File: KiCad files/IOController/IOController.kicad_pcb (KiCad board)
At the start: 2 copper layers, 22.5 x 68.6 mm, 31 parts, among them J1 AVR-ISP-6, J3 XT60 Horizontal Socket, J6 XT60 Horizontal Socket, Q1 BSS138, SW1 RotaryEncoder_Switch, SW2 SW_Push, U1 ATtiny85-20P, U3 LP2985-1.8, U4 LP2985-5.0

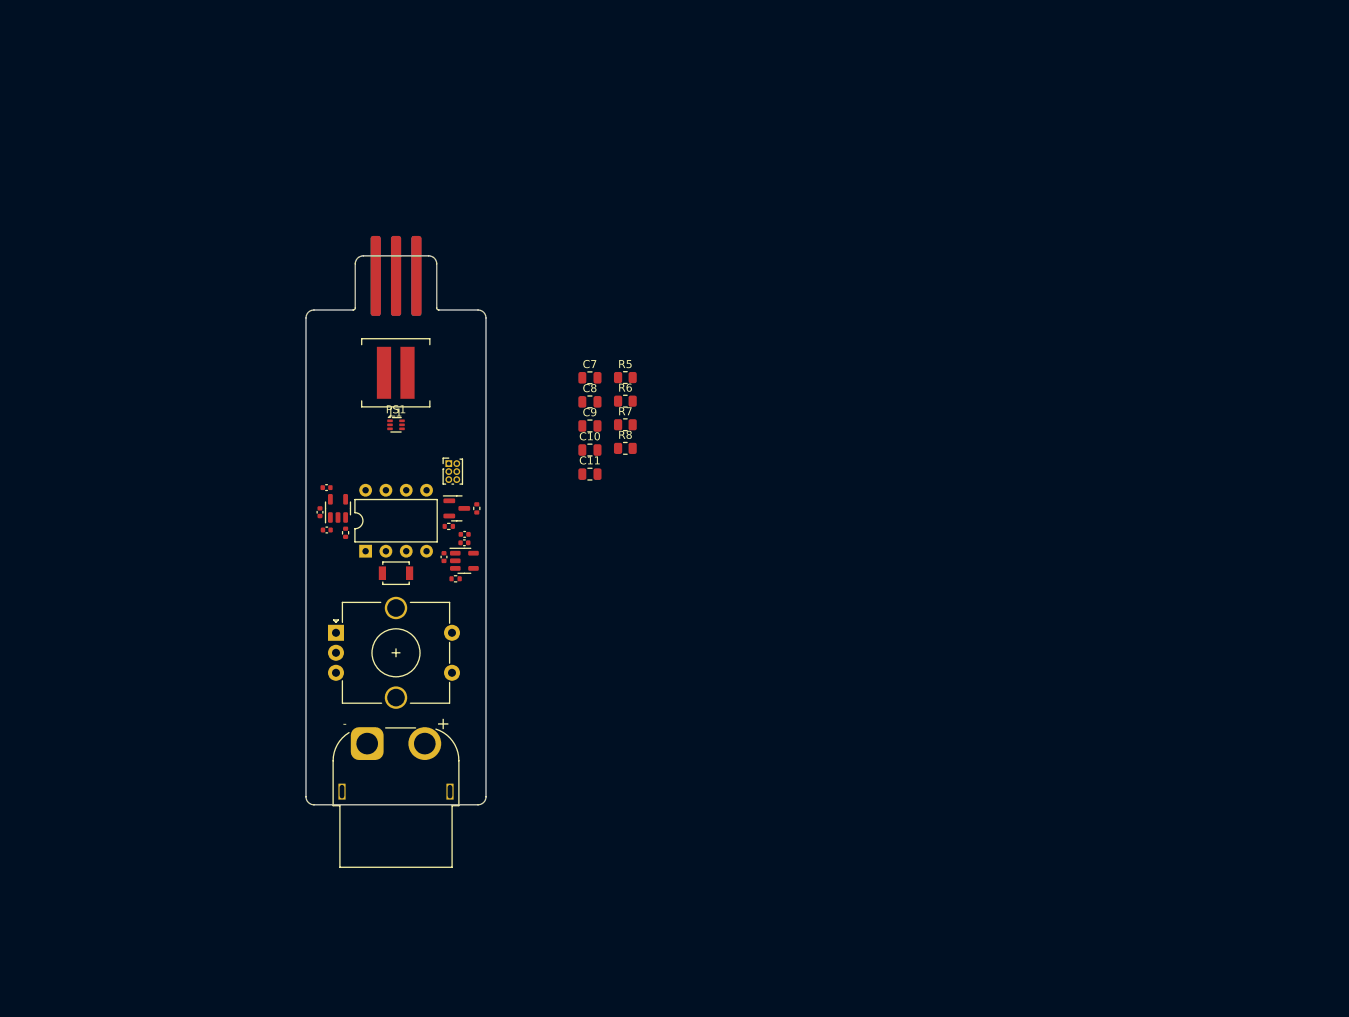
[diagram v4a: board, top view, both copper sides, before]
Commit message: started re-work of led driver circuit on IO board
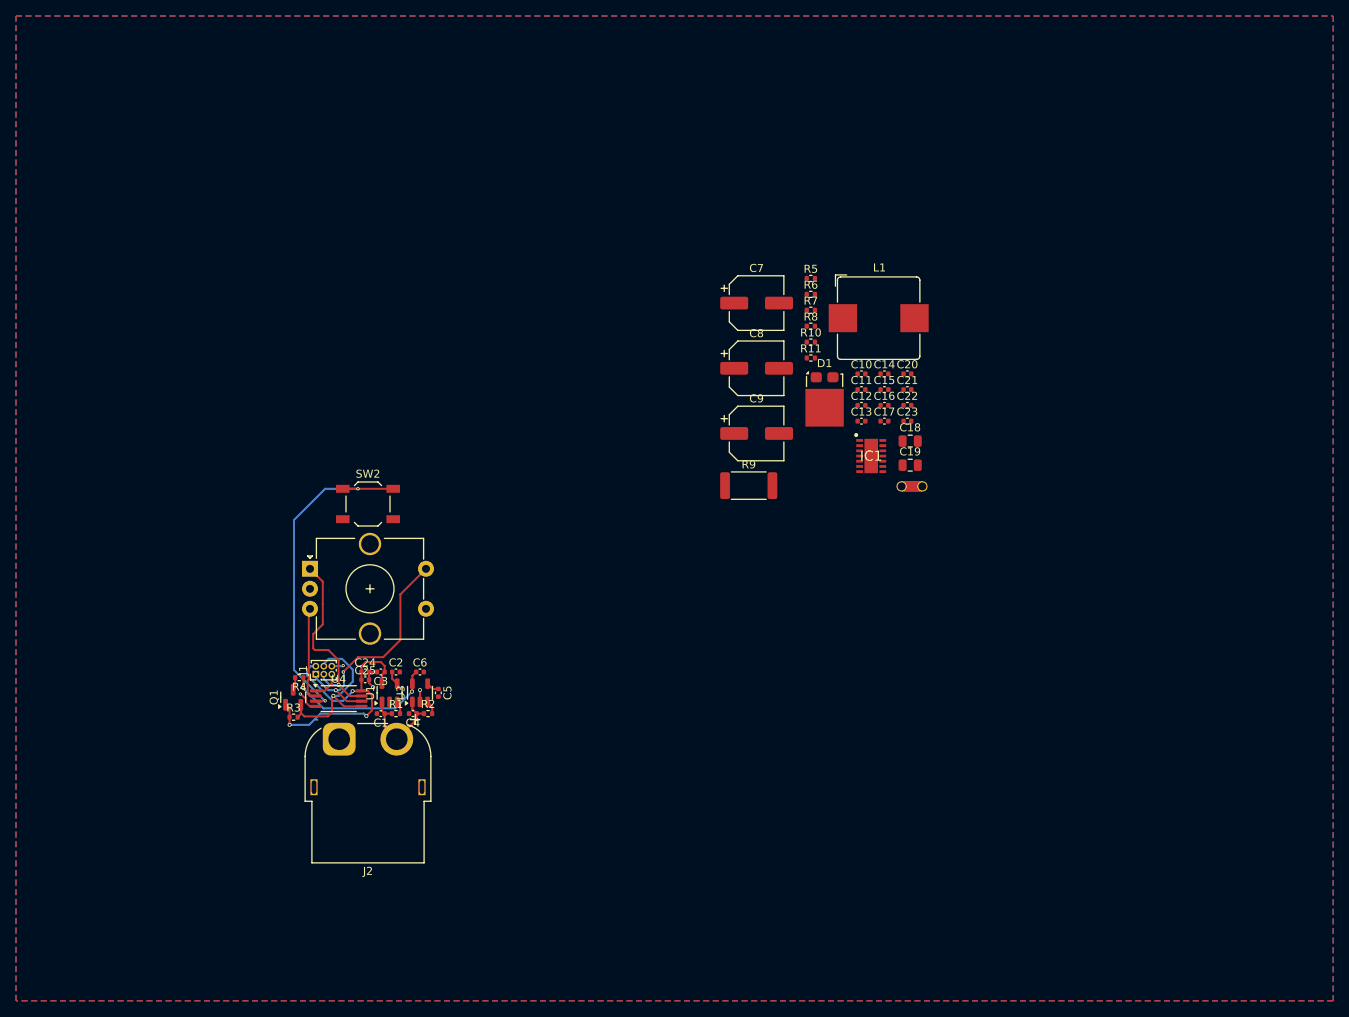
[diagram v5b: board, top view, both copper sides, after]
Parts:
- removed J3: XT60 Horizontal Socket, Connector_AMASS:AMASS_XT60PW-F_1x02_P7.20mm_Horizontal
- removed J6 (x2): XT60 Horizontal Socket, Connector_PinHeader_2.54mm:PinHeader_1x03_P2.54mm_Vertical
- removed PS1: TPS566242DRLR, Package_TO_SOT_SMD:SOT-563
- added C12: 25V 1uF 0402, Capacitor_SMD:C_0402_1005Metric, F.Cu at (90.7, 51.1)
- added C13: 25V 1uF 0402, Capacitor_SMD:C_0402_1005Metric, F.Cu at (90.7, 53.0)
- added C14: 25V 100nF 0402, Capacitor_SMD:C_0402_1005Metric, F.Cu at (93.6, 47.1)
- added C15: 10V 10nF 0402, Capacitor_SMD:C_0402_1005Metric, F.Cu at (93.6, 49.1)
- added C16: 10V 10nF 0402, Capacitor_SMD:C_0402_1005Metric, F.Cu at (93.6, 51.1)
- added C17: 16V 2.2uF 0402, Capacitor_SMD:C_0402_1005Metric, F.Cu at (93.6, 53.0)
- added C18: 50V 2.2uF 0805, Capacitor_SMD:C_0805_2012Metric, F.Cu at (96.8, 55.5)
- added C19: 50V 2.2uF 0805, Capacitor_SMD:C_0805_2012Metric, F.Cu at (96.8, 58.5)
- added C20: 50V 1uF 0402, Capacitor_SMD:C_0402_1005Metric, F.Cu at (96.4, 47.1)
- added C21: 50V 1uF 0402, Capacitor_SMD:C_0402_1005Metric, F.Cu at (96.4, 49.1)
- added C22: 50V 100nF 402, Capacitor_SMD:C_0402_1005Metric, F.Cu at (96.4, 51.1)
- added C23: 50V 100nF 402, Capacitor_SMD:C_0402_1005Metric, F.Cu at (96.4, 53.0)
- added C24: 0.1uF 0402, Capacitor_SMD:C_0402_1005Metric, F.Cu at (28.7, 84.4)
- added C25: 1uF 0402, Capacitor_SMD:C_0402_1005Metric, F.Cu at (28.7, 85.4)
- added D1: FSV12100V, Package_TO_SOT_SMD:TO-277A, F.Cu at (86.1, 50.3)
- added IC1: TPS922054DMTR, TPS922054DMTR:SON65P300X450X100-15N-D, F.Cu at (91.9, 57.4)
- added J2: XT60 Horizontal Socket, Connector_AMASS:AMASS_XT60PW-F_1x02_P7.20mm_Horizontal, F.Cu at (25.4, 92.8)
- added NTe1: NetTie_2, NetTie:NetTie-2_THT_Pad1.0mm, F.Cu at (95.7, 61.2)
- added R10: 309K 0402, Resistor_SMD:R_0402_1005Metric, F.Cu at (84.4, 43.2)
- added R11: 102K 0402, Resistor_SMD:R_0402_1005Metric, F.Cu at (84.4, 45.2)
- added R9: 33mΩ 2512, Resistor_SMD:R_2512_6332Metric, F.Cu at (76.6, 61.1)
- C1, C4: value 0402 1uF -> 1uF 0402
- C10: value 22uF -> 50V 100nF 402; footprint Capacitor_SMD:C_0805_2012Metric -> Capacitor_SMD:C_0402_1005Metric
- C11: value 100nF -> 50V 100nF 402; footprint Capacitor_SMD:C_0805_2012Metric -> Capacitor_SMD:C_0402_1005Metric
- C2, C5: value 0402 10nF -> 10nF 0402
- C3, C6: value 0402 2.2uF -> 2.2uF 0402
- C7: value 10uF 0805 -> 50V 68uF D6.3; footprint Capacitor_SMD:C_0805_2012Metric -> Capacitor_SMD:CP_Elec_6.3x5.9
- C8: value 100nF 0805 -> 50V 22uF D6.3; footprint Capacitor_SMD:C_0805_2012Metric -> Capacitor_SMD:CP_Elec_6.3x5.9
- C9: value 100nF -> 50V 22uF D6.3; footprint Capacitor_SMD:C_0805_2012Metric -> Capacitor_SMD:CP_Elec_6.3x5.9
- L1: value MDA7030-2R2M -> 10uH SRP1038WA; footprint Inductor_SMD:L_Coilcraft_XAL7030-222 -> Inductor_SMD:L_Bourns_SRP1038C_10.0x10.0mm
- R5: value 100K 0805 -> 10K 0402; footprint Resistor_SMD:R_0805_2012Metric -> Resistor_SMD:R_0402_1005Metric
- R6: value 23.2K 0805 -> 52K3 0402; footprint Resistor_SMD:R_0805_2012Metric -> Resistor_SMD:R_0402_1005Metric
- R7: value 120K 0805 -> 61K9 0402; footprint Resistor_SMD:R_0805_2012Metric -> Resistor_SMD:R_0402_1005Metric
- R8: value 30K 0805 -> 825ohm 0402; footprint Resistor_SMD:R_0805_2012Metric -> Resistor_SMD:R_0402_1005Metric
- SW2: value SW_Push -> TL3342; footprint Button_Switch_SMD:SW_SPST_B3U-1000P -> Button_Switch_SMD:SW_SPST_TL3342
- U1: value ATtiny85-20P -> LP2985-1.8; footprint Package_DIP:DIP-8_W7.62mm -> Package_TO_SOT_SMD:SOT-23-5
- U3: value LP2985-1.8 -> LP2985-5.0
- U4: value LP2985-5.0 -> ATtiny45V-10X; footprint Package_TO_SOT_SMD:SOT-23-5 -> Package_SO:TSSOP-8_4.4x3mm_P0.65mm
- moved L1 60.8 mm to (92.8, 40.2), turned to 0 degrees
- moved C11 35.5 mm to (90.7, 49.1)
- moved C10 35.3 mm to (90.7, 47.1)
- moved Q1 31.2 mm to (19.6, 87.6), turned to 90 degrees
- moved J1 31.1 mm to (22.5, 84.7), turned to 90 degrees
- moved R3 30.7 mm to (19.7, 90.0)
- moved R4 30.7 mm to (20.4, 85.1), turned to 180 degrees
- moved R8 27.8 mm to (84.4, 41.2)
- moved R7 27.2 mm to (84.4, 39.2)
- moved R6 26.8 mm to (84.4, 37.2)
- moved R5 26.3 mm to (84.4, 35.2)
- moved U3 25.2 mm to (35.5, 87.0)
- moved C3 24.0 mm to (30.6, 84.4)
- moved C1 23.9 mm to (30.6, 89.6)
- moved R1 23.5 mm to (32.5, 89.6), turned to 0 degrees
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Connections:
- net NPN-Gate_5V renamed LED_PWM_5V
- C10 pad 1: VDD -> VCC
- C10 pad 2: GND -> GNDPWR
- C11 pad 1: VDD -> VCC
- C11 pad 2: GND -> GNDPWR
- C2 pad 1: Net-(U3-BP) -> Net-(U1-BP)
- C5 pad 1: Net-(U4-BP) -> Net-(U3-BP)
- C7 pad 2: GND -> GNDPWR
- C8 pad 2: GND -> GNDPWR
- C9 pad 1: VDD -> VCC
- C9 pad 2: Net-(PS1-FB) -> GNDPWR
- J1 pad 4: NPN-Gate_1.8V -> LED_PWM_1V8
- L1 pad 2: VDD -> Net-(IC1-CSN)
- Q1 pad 2: NPN-Gate_1.8V -> LED_PWM_1V8
- R1 pad 2: Net-(U3-ON/~{OFF}) -> Net-(U1-ON/~{OFF})
- R2 pad 2: Net-(U4-ON/~{OFF}) -> Net-(U3-ON/~{OFF})
- R3 pad 2: NPN-Gate_1.8V -> LED_PWM_1V8
- R5 pad 1: Net-(PS1-EN) -> VCC
- R5 pad 2: VCC -> Net-(IC1-ADIM/HD)
- R6 pad 1: Net-(PS1-EN) -> Net-(IC1-FSET)
- R7 pad 1: VDD -> Net-(IC1-TEMP)
- R7 pad 2: Net-(PS1-FB) -> GND
- R8 pad 1: Net-(PS1-FB) -> Net-(IC1-COMP)
- R8 pad 2: GND -> Net-(C15-Pad1)
- U1 pad 1: Net-(J1-~{RST}) -> VCC
- U1 pad 2: ROT_B -> GND
- U1 pad 3: SW1 -> Net-(U1-ON/~{OFF})
- U1 pad 4: GND -> Net-(U1-BP)
- U1 pad 5: NPN-Gate_1.8V -> +1V8
- U3 pad 5: +1V8 -> +5V
- U4 pad 1: VCC -> Net-(J1-~{RST})
- U4 pad 2: GND -> ROT_B
- U4 pad 3: Net-(U4-ON/~{OFF}) -> SW1
- U4 pad 4: Net-(U4-BP) -> GND
- U4 pad 5: +5V -> LED_PWM_1V8
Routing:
- net SW1: track 0.00 -> 43.3 mm, vias 0 -> 2
- net +1V8: track 0.00 -> 36.8 mm, vias 0 -> 3
- net ROT_SW1: track 0.00 -> 29.4 mm, vias 0 -> 2
- net ROT_A: track 0.00 -> 24.2 mm, vias 0 -> 1
- net LED_PWM_1V8: track 0.00 -> 22.6 mm, vias 0 -> 1
- net +5V: track 0.00 -> 19.5 mm, vias 0 -> 2
- net VCC: track 0.00 -> 13.2 mm
- net ROT_B: track 0.00 -> 11.9 mm
- net GND: track 0.00 -> 8.85 mm, vias 0 -> 4
- net Net-(J1-~{RST}): track 0.00 -> 3.56 mm
- net Net-(U1-BP): track 0.00 -> 1.72 mm
- net Net-(U3-ON/~{OFF}): track 0.00 -> 1.70 mm
- net LED_PWM_5V: track 0.00 -> 1.63 mm
- net Net-(U3-BP): track 0.00 -> 1.62 mm
- net Net-(U1-ON/~{OFF}): track 0.00 -> 1.61 mm
- added copper zone on B.Cu, net GND
- added copper zone on F.Cu, net GND
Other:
- board outline removed

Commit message: completed circuit, could be laid out better
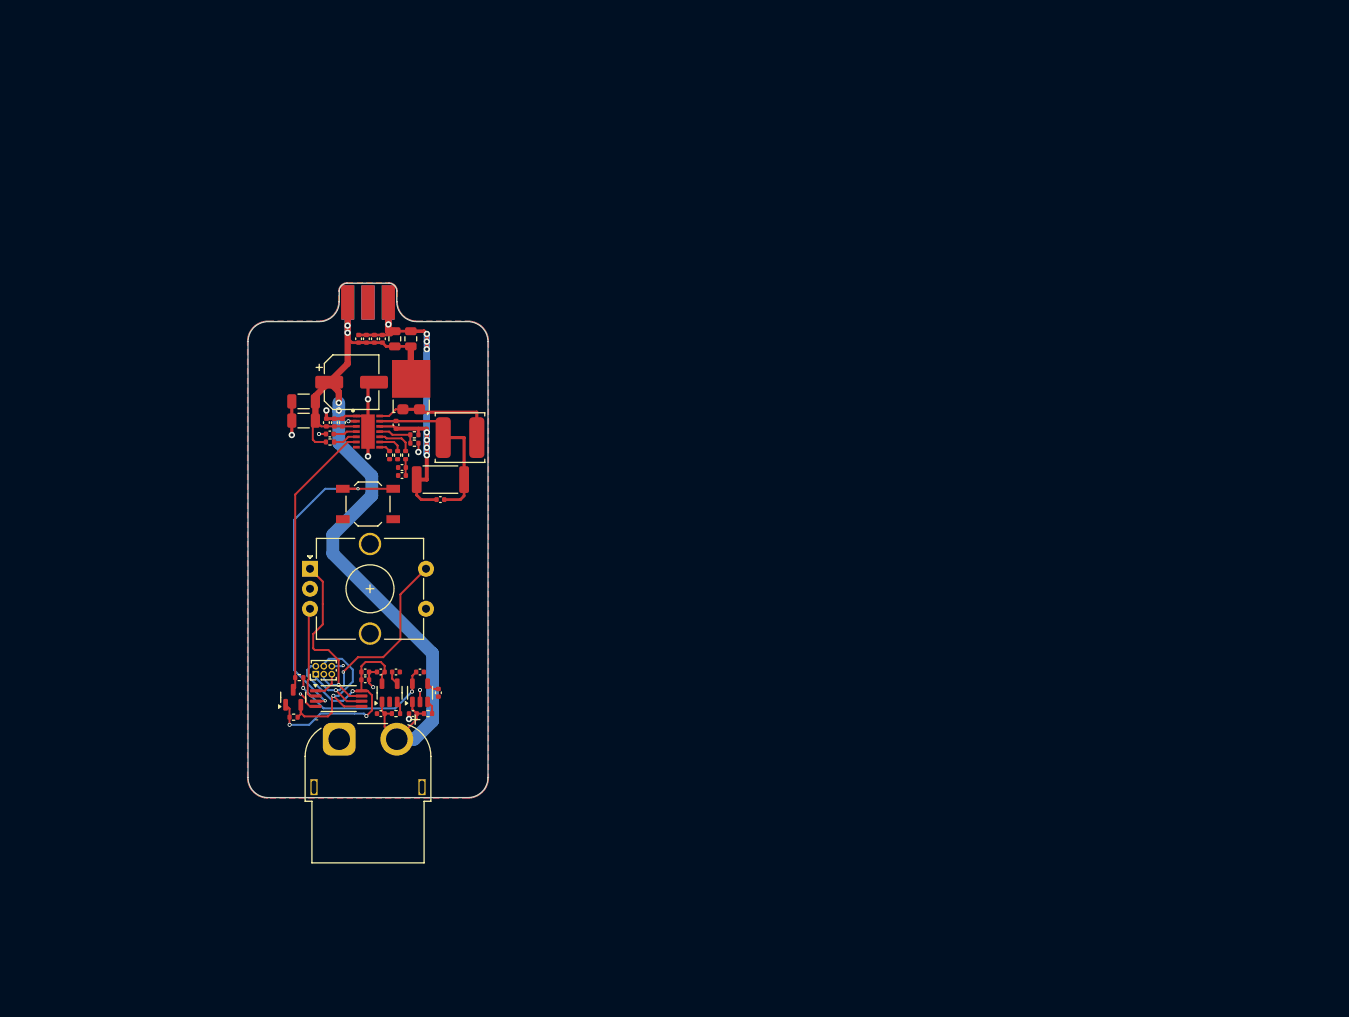
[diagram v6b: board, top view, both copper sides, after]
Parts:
- removed NTe1: NetTie_2, NetTie:NetTie-2_THT_Pad1.0mm
- added J3: edge connector, EnvExtras:CardEdge1x03, F.Cu at (29.0, 38.2)
- C8, C9: value 50V 22uF D6.3 -> 35V 22uF 1206; footprint Capacitor_SMD:CP_Elec_6.3x5.9 -> Capacitor_SMD:C_1206_3216Metric
- L1: value 10uH SRP1038WA -> VLS6045AF-100M; footprint Inductor_SMD:L_Bourns_SRP1038C_10.0x10.0mm -> Inductor_SMD:L_TDK_VLS6045EX_VLS6045AF
- moved C20 68.7 mm to (27.8, 42.8), turned to 90 degrees
- moved C21 67.9 mm to (28.8, 42.8), turned to 90 degrees
- moved C10 67.2 mm to (23.8, 53.2), turned to 90 degrees
- moved C22 67.1 mm to (29.8, 42.8), turned to 90 degrees
- moved C13 66.5 mm to (24.2, 54.6)
- moved C23 66.4 mm to (30.8, 42.8), turned to 90 degrees
- moved C19 66.3 mm to (32.4, 42.8), turned to 90 degrees
- moved C11 66.0 mm to (24.8, 53.2), turned to 90 degrees
- moved C12 64.9 mm to (25.8, 53.2), turned to 90 degrees
- moved C18 63.7 mm to (34.4, 42.7), turned to 90 degrees
- moved R5 63.5 mm to (24.2, 55.6)
- moved IC1 63.0 mm to (29.0, 54.4)
- moved C14 61.4 mm to (32.5, 53.5), turned to -90 degrees
- moved C15 61.1 mm to (33.2, 58.8), turned to 180 degrees
- moved C16 60.9 mm to (33.2, 59.8), turned to 180 degrees
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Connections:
- C10 pad 2: GNDPWR -> GND
- C11 pad 2: GNDPWR -> GND
- C12 pad 2: GNDPWR -> GND
- C18 pad 1: LED_V+ -> VCC
- C19 pad 1: LED_V+ -> VCC
- C20 pad 1: LED_V+ -> VCC
- C21 pad 1: LED_V+ -> VCC
- C22 pad 1: LED_V+ -> VCC
- C23 pad 1: LED_V+ -> VCC
- C7 pad 2: GNDPWR -> GND
- C8 pad 2: GNDPWR -> GND
- C9 pad 2: GNDPWR -> GND
- D1 pad 3: LED_V+ -> VCC
- IC1 pad 1: GNDPWR -> GND
- IC1 pad 15: GNDPWR -> GND
- R11 pad 1: GNDPWR -> GND
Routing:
- net VCC: track 13.2 -> 117.7 mm, vias 0 -> 4
- net LED_V-: track 0.00 -> 68.6 mm, vias 0 -> 8
- net LED_PWM_5V: track 1.63 -> 34.9 mm
- net GND: track 8.85 -> 35.1 mm, vias 4 -> 12
- net Net-(IC1-CSN): track 0.00 -> 22.6 mm
- net Net-(IC1-SW): track 0.00 -> 15.8 mm
- net Net-(IC1-UVP): track 0.00 -> 5.06 mm
- net Net-(IC1-COMP): track 0.00 -> 4.62 mm
- net Net-(IC1-FSET): track 0.00 -> 3.12 mm
- net Net-(IC1-ADIM/HD): track 0.00 -> 3.06 mm
- net Net-(IC1-VCC): track 0.00 -> 2.97 mm
- net Net-(C15-Pad1): track 0.00 -> 2.05 mm
- net Net-(IC1-TEMP): track 0.00 -> 1.45 mm
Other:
- board outline added: 30 x 64.3 mm

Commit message: laid out the circuit better but less space efficient.
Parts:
- C10, C11, C22, C23: value 50V 100nF 402 -> 50V 100nF 0805; footprint Capacitor_SMD:C_0402_1005Metric -> Capacitor_SMD:C_0805_2012Metric
- C20, C21: value 50V 1uF 0402 -> 50V 1uF 0805; footprint Capacitor_SMD:C_0402_1005Metric -> Capacitor_SMD:C_0805_2012Metric
- C7: value 50V 68uF D6.3 -> 35V 68uF; footprint Capacitor_SMD:CP_Elec_6.3x5.9 -> Capacitor_Tantalum_SMD:CP_EIA-7343-43_Kemet-X
- moved C17 26.9 mm to (35.5, 36.1), turned to 0 degrees
- moved C16 22.5 mm to (42.0, 39.0), turned to 0 degrees
- moved R9 21.9 mm to (35.5, 38.6), turned to 0 degrees
- moved C15 20.8 mm to (42.0, 40.0), turned to 0 degrees
- moved R6 18.7 mm to (42.0, 41.0), turned to 0 degrees
- moved R7 18.4 mm to (42.0, 42.0), turned to 0 degrees
- moved R5 18.2 mm to (41.0, 62.8), turned to 90 degrees
- moved C13 17.8 mm to (40.0, 62.8), turned to 90 degrees
- moved C12 16.3 mm to (39.0, 62.8), turned to -90 degrees
- moved C7 16.1 mm to (30.7, 63.9)
- moved SW2 15.9 mm to (17.2, 74.0), turned to -90 degrees
- moved R8 14.9 mm to (41.5, 44.6), turned to 90 degrees
- moved C8 12.6 mm to (29.0, 60.2), turned to 0 degrees
- moved L1 12.5 mm to (34.9, 43.9), turned to 90 degrees
- moved IC1 11.3 mm to (39.9, 57.6), turned to 90 degrees
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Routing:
- net LED_V-: track 68.6 -> 34.3 mm, vias 8 -> 2
- net GND: track 35.1 -> 9.53 mm, vias 12 -> 632
- net SW1: track 43.3 -> 20.0 mm
- net VCC: track 117.7 -> 101.9 mm
- net Net-(IC1-FSET): track 3.12 -> 18.3 mm
- net Net-(IC1-TEMP): track 1.45 -> 15.8 mm
- net LED_PWM_5V: track 34.9 -> 46.7 mm, vias 0 -> 2
- net Net-(IC1-COMP): track 4.62 -> 12.4 mm
- net Net-(C15-Pad1): track 2.05 -> 8.88 mm
- net Net-(IC1-CSN): track 22.6 -> 27.4 mm
- net Net-(IC1-UVP): track 5.06 -> 8.22 mm
- net Net-(IC1-SW): track 15.8 -> 14.9 mm
- net unconnected-(J3-Pin_2-Pad2): vias 0 -> 1
- added copper zone on F.Cu, net LED_V-
- added copper zone on F.Cu, net VCC
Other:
- board size 30 x 64.3 mm -> 30 x 74.3 mm
